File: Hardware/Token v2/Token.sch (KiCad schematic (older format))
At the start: 8 parts, among them J2 Conn_01x04_Female, J4 Conn_02x04_Odd_Even, U1 ATtiny202-SS

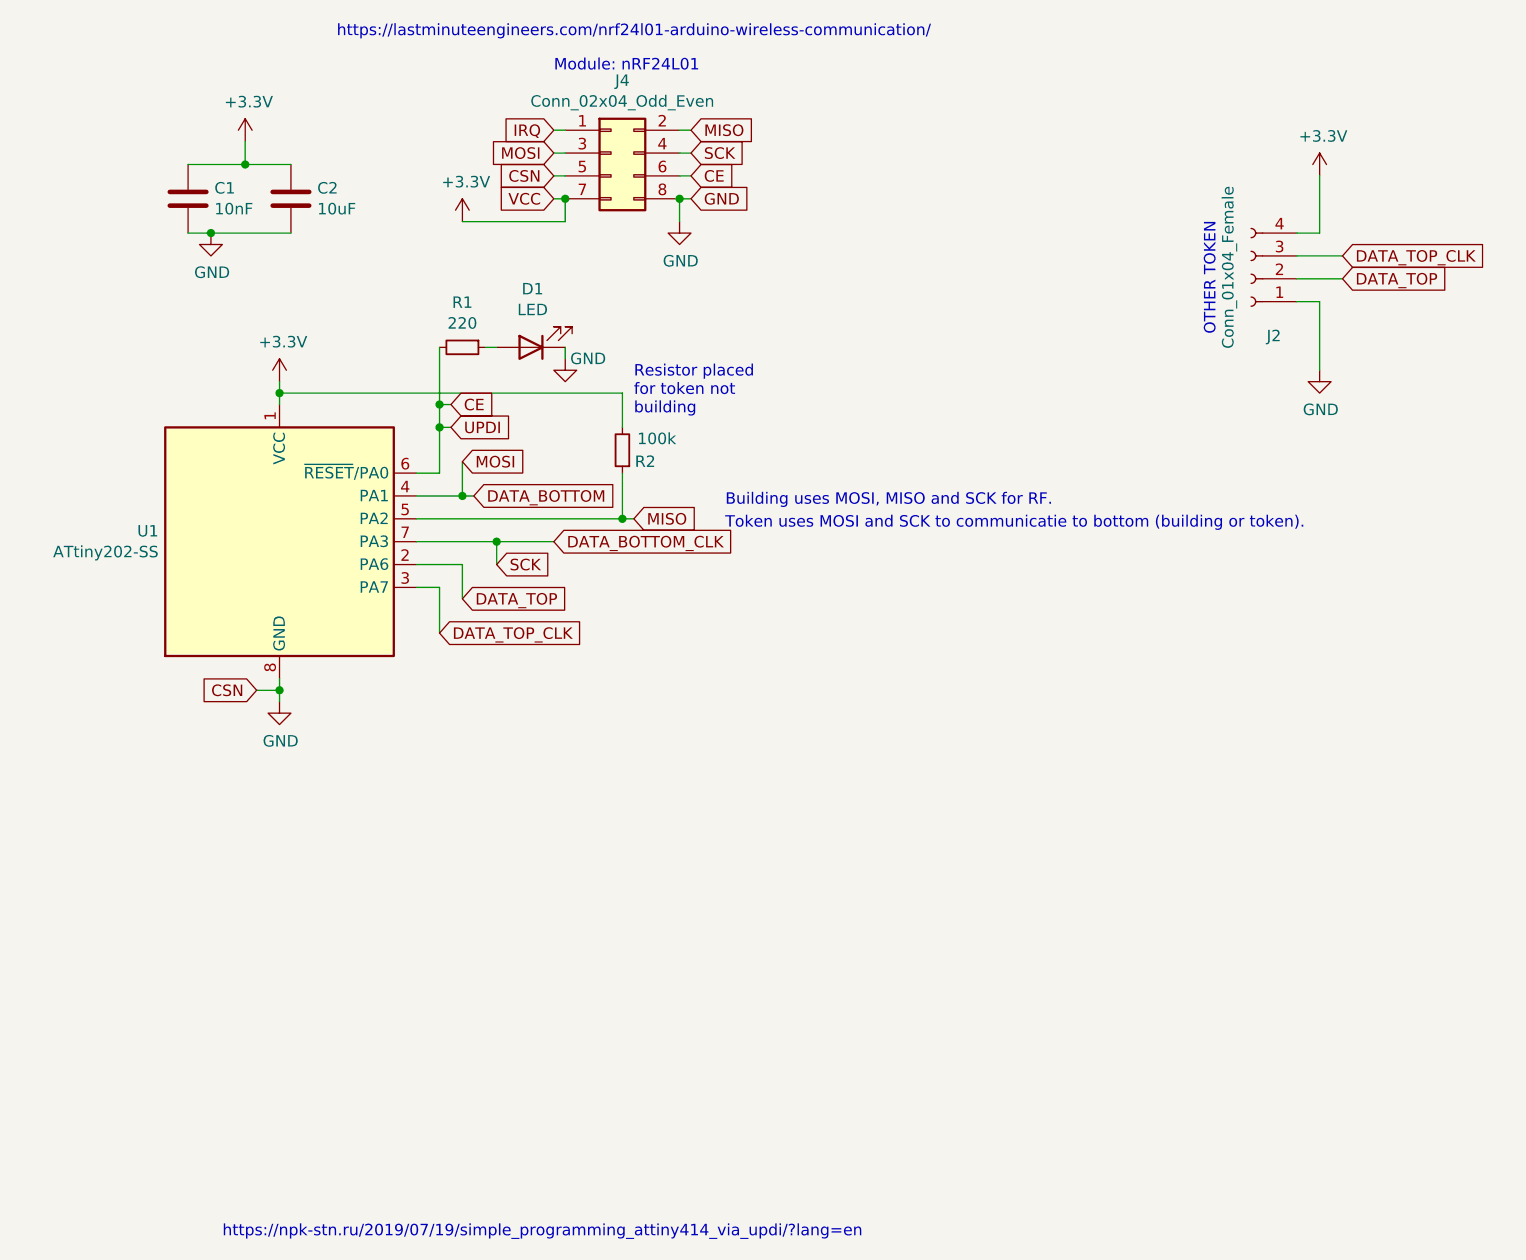
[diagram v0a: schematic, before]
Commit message: Created a new version of the hardware token v2
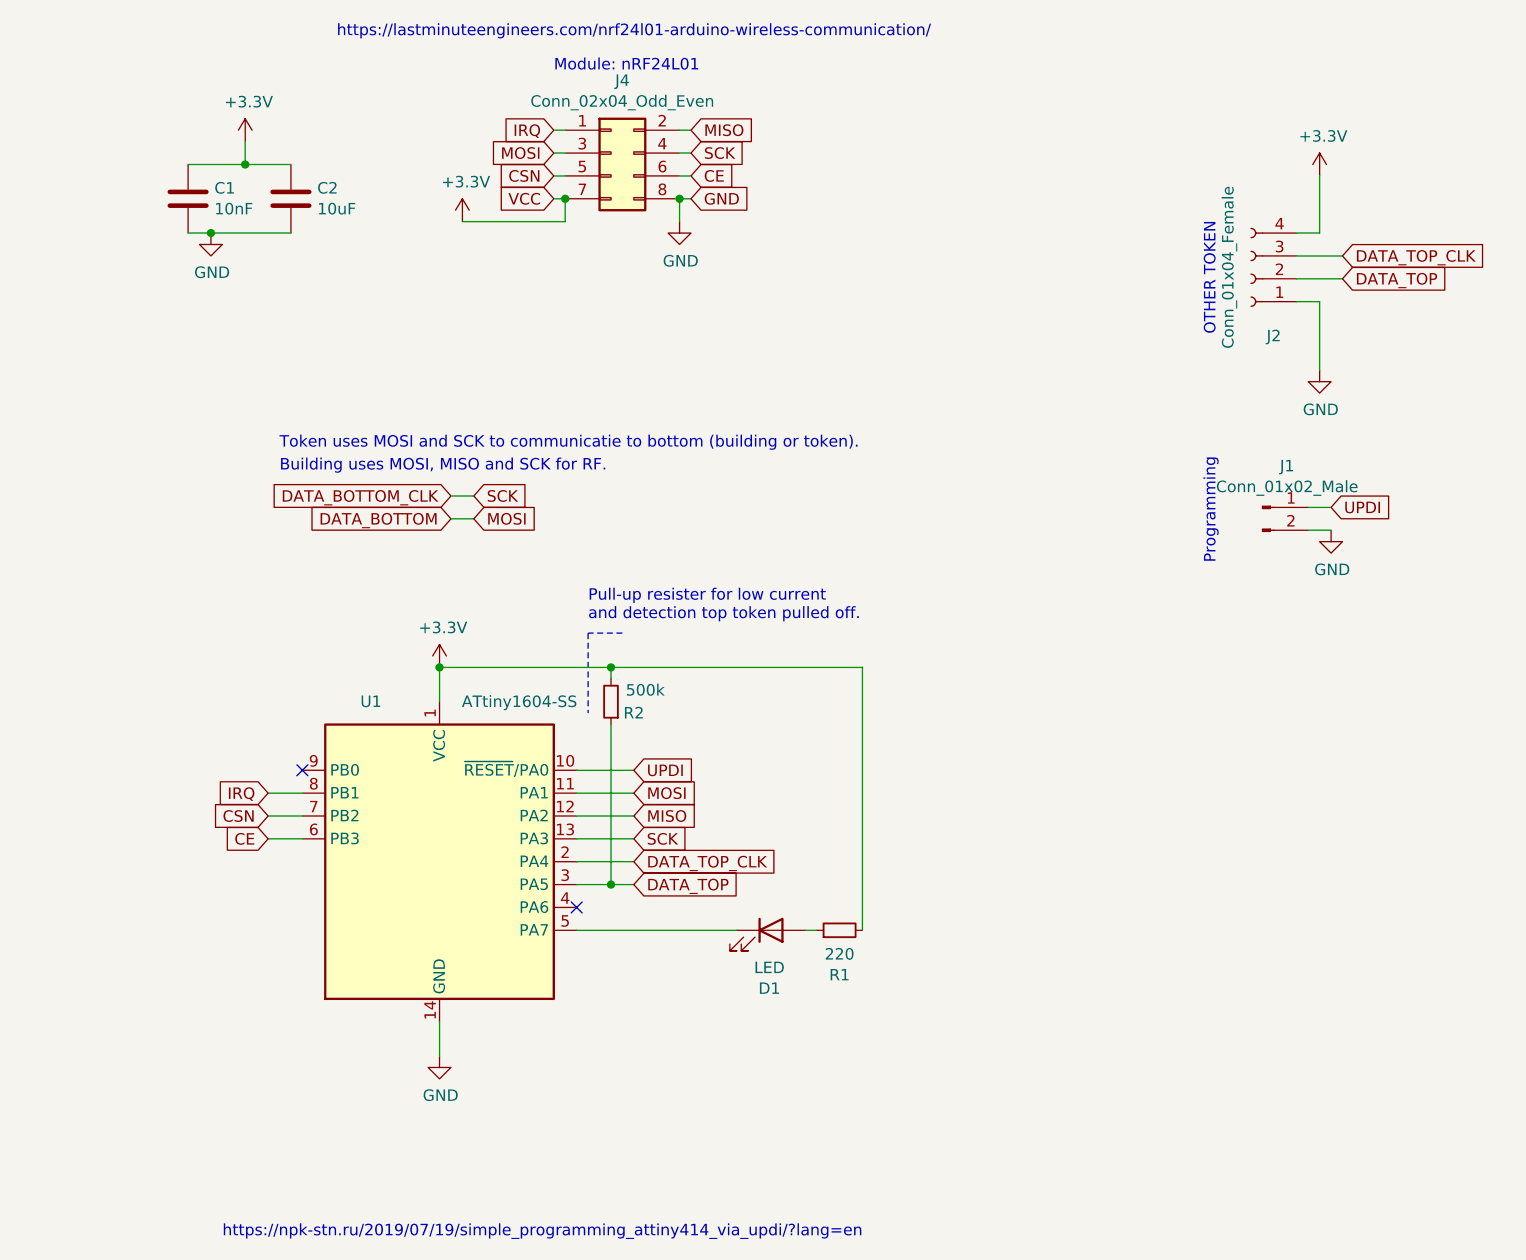
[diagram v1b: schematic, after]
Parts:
- removed U1: ATtiny202-SS, Package_SO:SOIC-8_3.9x4.9mm_P1.27mm, symbol MCU_Microchip_ATtiny:ATtiny202-SS
- added J1: Conn_01x02_Male, Connector_PinHeader_2.54mm:PinHeader_1x02_P2.54mm_Vertical, symbol Connector:Conn_01x02_Male
- added U1: ATtiny1604-SS, Package_SO:SOIC-14_3.9x8.7mm_P1.27mm, symbol MCU_Microchip_ATtiny:ATtiny1604-SS
- R1: footprint Resistor_SMD:R_1206_3216Metric_Pad1.30x1.75mm_HandSolder -> Resistor_SMD:R_0805_2012Metric_Pad1.20x1.40mm_HandSolder
- R2: value 100k -> 500k
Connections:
- net +3V3: now also R1.2, U1.1 (VCC)
- net CE: now also U1.6 (PB3); no longer R1.2
- net DATA_BOTTOM: now also U1.11 (PA1)
- net DATA_BOTTOM_CLK: now also U1.13 (PA3)
- net DATA_TOP: now also R2.1, U1.3 (PA5)
- net DATA_TOP_CLK: now also U1.2 (PA4)
- net GND: now also J1.2 (Pin_2), U1.14 (GND); no longer D1.1 (K), J4.5 (Pin_5)
- net IRQ: now also U1.8 (PB1)
- net MISO: now also U1.12 (PA2); no longer R2.1
- new net: D1.1 (K), U1.5 (PA7)
- new net CSN: J4.5 (Pin_5), U1.7 (PB2)
- new net UPDI: J1.1 (Pin_1), U1.10 (~RESET~/PA0)
- no-connect marks 0 -> 2
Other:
- note added: "Programming"
- note added: "Pull-up resister for low current\nand detection top token pulled off."
- note removed: "Resistor placed\nfor token not\nbuilding"
- moved on the sheet: D1, R1, R2
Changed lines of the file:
@@
 Sheet 1 1
 Title "ELC - Team RED Token Infrastructure"
-Date "2021-03-23"
-Rev "2.0"
+Date "2021-04-09"
+Rev "2.1"
 Comp "Avans Hogeschool"
 Comment1 "Expertise Centrum Technische Innovatie"
@@
 Text Notes 1500 7400 0    50   ~ 0
 https://npk-stn.ru/2019/07/19/simple_programming_attiny414_via_updi/?lang=en
-$Comp
-L MCU_Microchip_ATtiny:ATtiny202-SS U1
-U 1 1 605A875E
-P 1750 4350
-F 0 "U1" H 1221 4396 50  0000 R CNN
-F 1 "ATtiny202-SS" H 1221 4305 50  0000 R CNN
-F 2 "Package_SO:SOIC-8_3.9x4.9mm_P1.27mm" H 1750 4350 50  0001 C CIN
-F 3 "http://ww1.microchip.com/downloads/en/DeviceDoc/ATtiny202-402-AVR-MCU-with-Core-Independent-Peripherals_and-picoPower-40001969A.pdf" H 1750 4350 50  0001 C CNN
-	1    1750 4350
-	1    0    0    -1
-$EndComp
-Text GLabel 2500 3850 2    50   Input ~ 0
+Text GLabel 3300 5350 2    50   Input ~ 0
 UPDI
-Wire Wire Line
-	2350 4050 2450 4050
-Text GLabel 2550 4000 2    50   Input ~ 0
+Text GLabel 3300 5450 2    50   Input ~ 0
 MOSI
-Text GLabel 3300 4250 2    50   Input ~ 0
+Text GLabel 3300 5550 2    50   Input ~ 0
 MISO
-Text GLabel 2700 4450 2    50   Input ~ 0
+Text GLabel 3300 5650 2    50   Input ~ 0
 SCK
-Text GLabel 2600 4150 2    50   Input ~ 0
+Text GLabel 2500 4250 0    50   Input ~ 0
 DATA_BOTTOM
-Text GLabel 2450 4750 2    50   Input ~ 0
+Text GLabel 3300 5750 2    50   Input ~ 0
 DATA_TOP_CLK
-Text GLabel 2950 4350 2    50   Input ~ 0
+Text GLabel 2500 4150 0    50   Input ~ 0
 DATA_BOTTOM_CLK
-Wire Wire Line
-	2550 4150 2550 4000
-Wire Wire Line
-	2350 4150 2550 4150
-Text GLabel 2550 4600 2    50   Input ~ 0
+Text GLabel 3300 5850 2    50   Input ~ 0
 DATA_TOP
-Wire Wire Line
-	2350 4550 2450 4550
-Wire Wire Line
-	2600 4150 2550 4150
-Connection ~ 2550 4150
-Wire Wire Line
-	2350 4450 2550 4450
-Wire Wire Line
-	2550 4450 2550 4600
-Wire Wire Line
-	2450 4550 2450 4750
-Wire Wire Line
-	2700 4350 2700 4450
-Wire Wire Line
-	2350 4350 2700 4350
-Wire Wire Line
-	2950 4350 2700 4350
-Connection ~ 2700 4350
 $Comp
 L Device:R_Small R2
 U 1 1 605C3635
-P 3250 3950
-F 0 "R2" H 3150 4000 50  0000 C CNN
-F 1 "100k" H 3100 3900 50  0000 C CNN
-F 2 "Resistor_SMD:R_1206_3216Metric_Pad1.30x1.75mm_HandSolder" H 3250 3950 50  0001 C CNN
-F 3 "~" H 3250 3950 50  0001 C CNN
-	1    3250 3950
+P 3200 5050
+F 0 "R2" H 3100 5100 50  0000 C CNN
+F 1 "500k" H 3050 5000 50  0000 C CNN
+F 2 "Resistor_SMD:R_1206_3216Metric_Pad1.30x1.75mm_HandSolder" H 3200 5050 50  0001 C CNN
+F 3 "~" H 3200 5050 50  0001 C CNN
+	1    3200 5050
 	-1   0    0    1
 $EndComp
@@
 L power:+3.3V #PWR01
 U 1 1 605C63C4
-P 1750 3650
-F 0 "#PWR01" H 1750 3500 50  0001 C CNN
-F 1 "+3.3V" H 1765 3823 50  0000 C CNN
-F 2 "" H 1750 3650 50  0001 C CNN
-F 3 "" H 1750 3650 50  0001 C CNN
-	1    1750 3650
-	1    0    0    -1
-$EndComp
-Wire Wire Line
-	1750 3650 1750 3700
-$Comp
-L power:GND #PWR02
-U 1 1 605C885B
-P 1750 5050
-F 0 "#PWR02" H 1750 4800 50  0001 C CNN
-F 1 "GND" H 1755 4877 50  0000 C CNN
-F 2 "" H 1750 5050 50  0001 C CNN
-F 3 "" H 1750 5050 50  0001 C CNN
-	1    1750 5050
-	1    0    0    -1
-$EndComp
-Wire Wire Line
-	1750 4950 1750 5000
-Wire Wire Line
-	3250 3850 3250 3700
-Wire Wire Line
-	3250 3700 1750 3700
-Connection ~ 1750 3700
-Wire Wire Line
-	1750 3700 1750 3750
-Wire Wire Line
-	2350 4250 3250 4250
-Wire Wire Line
-	3250 4050 3250 4250
-Connection ~ 3250 4250
-Wire Wire Line
-	3250 4250 3300 4250
-Text Notes 3300 3800 0    50   ~ 0
-Resistor placed\nfor token not\nbuilding
-Text Notes 3700 4200 0    50   ~ 0
+P 2450 4900
+F 0 "#PWR01" H 2450 4750 50  0001 C CNN
+F 1 "+3.3V" H 2465 5073 50  0000 C CNN
+F 2 "" H 2450 4900 50  0001 C CNN
+F 3 "" H 2450 4900 50  0001 C CNN
+	1    2450 4900
+	1    0    0    -1
+$EndComp
+Text Notes 3100 4700 0    50   ~ 0
+Pull-up resister for low current\nand detection top token pulled off.
+Text Notes 1750 4050 0    50   ~ 0
 Building uses MOSI, MISO and SCK for RF.
-Text Notes 3700 4300 0    50   ~ 0
+Text Notes 1750 3950 0    50   ~ 0
 Token uses MOSI and SCK to communicatie to bottom (building or token).
 $Comp
 L Device:R_Small R1
 U 1 1 605D300C
-P 2550 3500
-F 0 "R1" V 2354 3500 50  0000 C CNN
-F 1 "220" V 2445 3500 50  0000 C CNN
-F 2 "Resistor_SMD:R_1206_3216Metric_Pad1.30x1.75mm_HandSolder" H 2550 3500 50  0001 C CNN
-F 3 "~" H 2550 3500 50  0001 C CNN
-	1    2550 3500
-	0    1    1    0
+P 4200 6050
+F 0 "R1" V 4004 6050 50  0000 C CNN
+F 1 "220" V 4095 6050 50  0000 C CNN
+F 2 "Resistor_SMD:R_0805_2012Metric_Pad1.20x1.40mm_HandSolder" H 4200 6050 50  0001 C CNN
+F 3 "~" H 4200 6050 50  0001 C CNN
+	1    4200 6050
+	0    -1   -1   0
 $EndComp
 $Comp
 L Device:LED D1
 U 1 1 605D332F
-P 2850 3500
-F 0 "D1" H 2843 3245 50  0000 C CNN
-F 1 "LED" H 2843 3336 50  0000 C CNN
-F 2 "Inductor_SMD:L_1206_3216Metric_Pad1.22x1.90mm_HandSolder" H 2850 3500 50  0001 C CNN
-F 3 "~" H 2850 3500 50  0001 C CNN
-	1    2850 3500
-	-1   0    0    1
-$EndComp
-$Comp
-L power:GND #PWR011
-U 1 1 605D41CE
-P 3000 3550
-F 0 "#PWR011" H 3000 3300 50  0001 C CNN
-F 1 "GND" H 3100 3550 50  0000 C CNN
-F 2 "" H 3000 3550 50  0001 C CNN
-F 3 "" H 3000 3550 50  0001 C CNN
-	1    3000 3550
-	1    0    0    -1
-$EndComp
-Wire Wire Line
-	3000 3500 3000 3550
-Wire Wire Line
-	2700 3500 2650 3500
-Wire Wire Line
-	2450 4050 2450 3850
-Wire Wire Line
-	2500 3850 2450 3850
-Connection ~ 2450 3850
-Wire Wire Line
-	2450 3850 2450 3750
+P 3900 6050
+F 0 "D1" H 3893 5795 50  0000 C CNN
+F 1 "LED" H 3893 5886 50  0000 C CNN
+F 2 "Inductor_SMD:L_1206_3216Metric_Pad1.22x1.90mm_HandSolder" H 3900 6050 50  0001 C CNN
+F 3 "~" H 3900 6050 50  0001 C CNN
+	1    3900 6050
+	1    0    0    -1
+$EndComp
+Wire Wire Line
+	4050 6050 4100 6050
 Text Notes 2000 2150 0    50   ~ 0
 https://lastminuteengineers.com/nrf24l01-arduino-wireless-communication/
-Text GLabel 2500 3750 2    50   Input ~ 0
+Text GLabel 1700 5650 0    50   Input ~ 0
 CE
-Wire Wire Line
-	2500 3750 2450 3750
-Connection ~ 2450 3750
-Wire Wire Line
-	2450 3750 2450 3500
-Text GLabel 1650 5000 0    50   Input ~ 0
-CSN
-Wire Wire Line
-	1650 5000 1750 5000
-Connection ~ 1750 5000
-Wire Wire Line
-	1750 5000 1750 5050
 Text GLabel 6400 3200 2    50   Input ~ 0
 DATA_TOP
@@
 Text GLabel 3550 2650 2    50   Input ~ 0
 SCK
+Text GLabel 1700 5550 0    50   Input ~ 0
+CSN
+$Comp
+L power:GND #PWR02
+U 1 1 60706721
+P 2450 6600
+F 0 "#PWR02" H 2450 6350 50  0001 C CNN
+F 1 "GND" H 2455 6427 50  0000 C CNN
+F 2 "" H 2450 6600 50  0001 C CNN
+F 3 "" H 2450 6600 50  0001 C CNN
+	1    2450 6600
+	1    0    0    -1
+$EndComp
+Wire Wire Line
+	2450 5050 2450 4900
+Connection ~ 2450 4900
+Wire Wire Line
+	3050 5450 3300 5450
+Wire Wire Line
+	3050 5550 3300 5550
+Wire Wire Line
+	3050 5650 3300 5650
+Wire Wire Line
+	4300 4900 3200 4900
+Wire Notes Line
+	3250 4750 3100 4750
+Wire Notes Line
+	3100 4750 3100 5100
+Wire Wire Line
+	2450 6450 2450 6600
+Text GLabel 2600 4150 2    50   Input ~ 0
+SCK
+Text GLabel 2600 4250 2    50   Input ~ 0
+MOSI
+Wire Wire Line
+	2500 4150 2600 4150
+Wire Wire Line
+	2600 4250 2500 4250
+Wire Wire Line
+	4300 4900 4300 6050
+Wire Wire Line
+	3750 6050 3050 6050
+Text GLabel 1700 5450 0    50   Input ~ 0
+IRQ
+Wire Wire Line
+	3200 4950 3200 4900
+Connection ~ 3200 4900
+Wire Wire Line
+	3200 4900 2450 4900
+Wire Wire Line
+	3200 5150 3200 5850
+Wire Wire Line
+	3200 5850 3050 5850
+Wire Wire Line
+	3300 5750 3050 5750
+Wire Wire Line
+	3300 5850 3200 5850
+Connection ~ 3200 5850
+Wire Wire Line
+	1700 5450 1850 5450
+Wire Wire Line
+	1700 5650 1850 5650
+NoConn ~ 1850 5350
+NoConn ~ 3050 5950
+$Comp
+L Connector:Conn_01x02_Male J1
+U 1 1 60740CD7
+P 6050 4200
+F 0 "J1" H 6158 4381 50  0000 C CNN
+F 1 "Conn_01x02_Male" H 6158 4290 50  0000 C CNN
+F 2 "Connector_PinHeader_2.54mm:PinHeader_1x02_P2.54mm_Vertical" H 6050 4200 50  0001 C CNN
+F 3 "~" H 6050 4200 50  0001 C CNN
+	1    6050 4200
+	1    0    0    -1
+$EndComp
+Text Notes 5850 4450 1    50   ~ 0
+Programming
+Wire Wire Line
+	3050 5350 3300 5350
+$Comp
+L MCU_Microchip_ATtiny:ATtiny1604-SS U1
+U 1 1 60700A84
+P 2450 5750
+F 0 "U1" H 2150 6450 50  0000 C CNN
+F 1 "ATtiny1604-SS" H 2800 6450 50  0000 C CNN
+F 2 "Package_SO:SOIC-14_3.9x8.7mm_P1.27mm" H 2450 5750 50  0001 C CIN
+F 3 "http://ww1.microchip.com/downloads/en/DeviceDoc/ATtiny804_1604-Data-Sheet-40002028A.pdf" H 2450 5750 50  0001 C CNN
+	1    2450 5750
+	1    0    0    -1
+$EndComp
+Wire Wire Line
+	1850 5550 1700 5550
+Text GLabel 6350 4200 2    50   Input ~ 0
+UPDI
+$Comp
+L power:GND #PWR03
+U 1 1 607420F5
+P 6350 4300
+F 0 "#PWR03" H 6350 4050 50  0001 C CNN
+F 1 "GND" H 6355 4127 50  0000 C CNN
+F 2 "" H 6350 4300 50  0001 C CNN
+F 3 "" H 6350 4300 50  0001 C CNN
+	1    6350 4300
+	1    0    0    -1
+$EndComp
+Wire Wire Line
+	6350 4300 6250 4300
+Wire Wire Line
+	6250 4200 6350 4200
 $EndSCHEMATC
